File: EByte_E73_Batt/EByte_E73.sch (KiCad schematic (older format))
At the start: 14 parts, among them J1 USB_OTG, J2 Serial Connector, U1 E73-2G4M04S, U2 ProMicro, U3 AP2112K-3.3, U4 CP2102N-A01-GQFN24, U5 MCP73831-2-OT

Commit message: completed V2.0
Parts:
- removed U4: CP2102N-A01-GQFN24, Housings_DFN_QFN:QFN-24-1EP_4x4mm_Pitch0.5mm, symbol CP2102N-A01-GQFN24
- removed U5: MCP73831-2-OT, TO_SOT_Packages_SMD:SOT-23-5_HandSoldering, symbol MCP73831-2-OT
- added C5, C7, C8: 10uF, Capacitors_SMD:C_0805_HandSoldering, symbol C
- added C6: 1nF, Capacitors_SMD:C_0805_HandSoldering, symbol C
- added C9: 0.1uF, Capacitors_SMD:C_0805_HandSoldering, symbol C
- added D1: MBR120, Diodes_SMD:D_SOD-123, symbol MBR0520
- added J3: Conn_01x02, Pin_Headers:Pin_Header_Straight_1x02_Pitch2.54mm, symbol Conn_01x02
- added JP1: JUMPER-SMT_2_NO, E73:SolderJumperSingle, symbol JUMPER-SMT_2_NO
- added Q1: DMG3415U, TO_SOT_Packages_SMD:SOT-23, symbol BSS83P
- added R2: 100K, Resistors_SMD:R_0805_HandSoldering, symbol R
- added R3: 10K, Resistors_SMD:R_0805_HandSoldering, symbol R
- added R4: 806K, Resistors_SMD:R_0805_HandSoldering, symbol R
- added R5: 2M, Resistors_SMD:R_0805_HandSoldering, symbol R
- added R6: 1K, Resistors_SMD:R_0805_HandSoldering, symbol R
- added U4: CH340C, SMD_Packages:SO-16-N, symbol CH340C
- added U6: TP4056, Power_Integrations:SO-8, symbol TP4056
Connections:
- net labels added: DTR, Data+, Data-, VBatt, VBus
- wire segments 94 -> 156
- no-connect marks 2 -> 10
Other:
- note added: "LiPo Charging\n"
- note added: "Power and Filtering"
- moved on the sheet: J1, J2, R1, U3

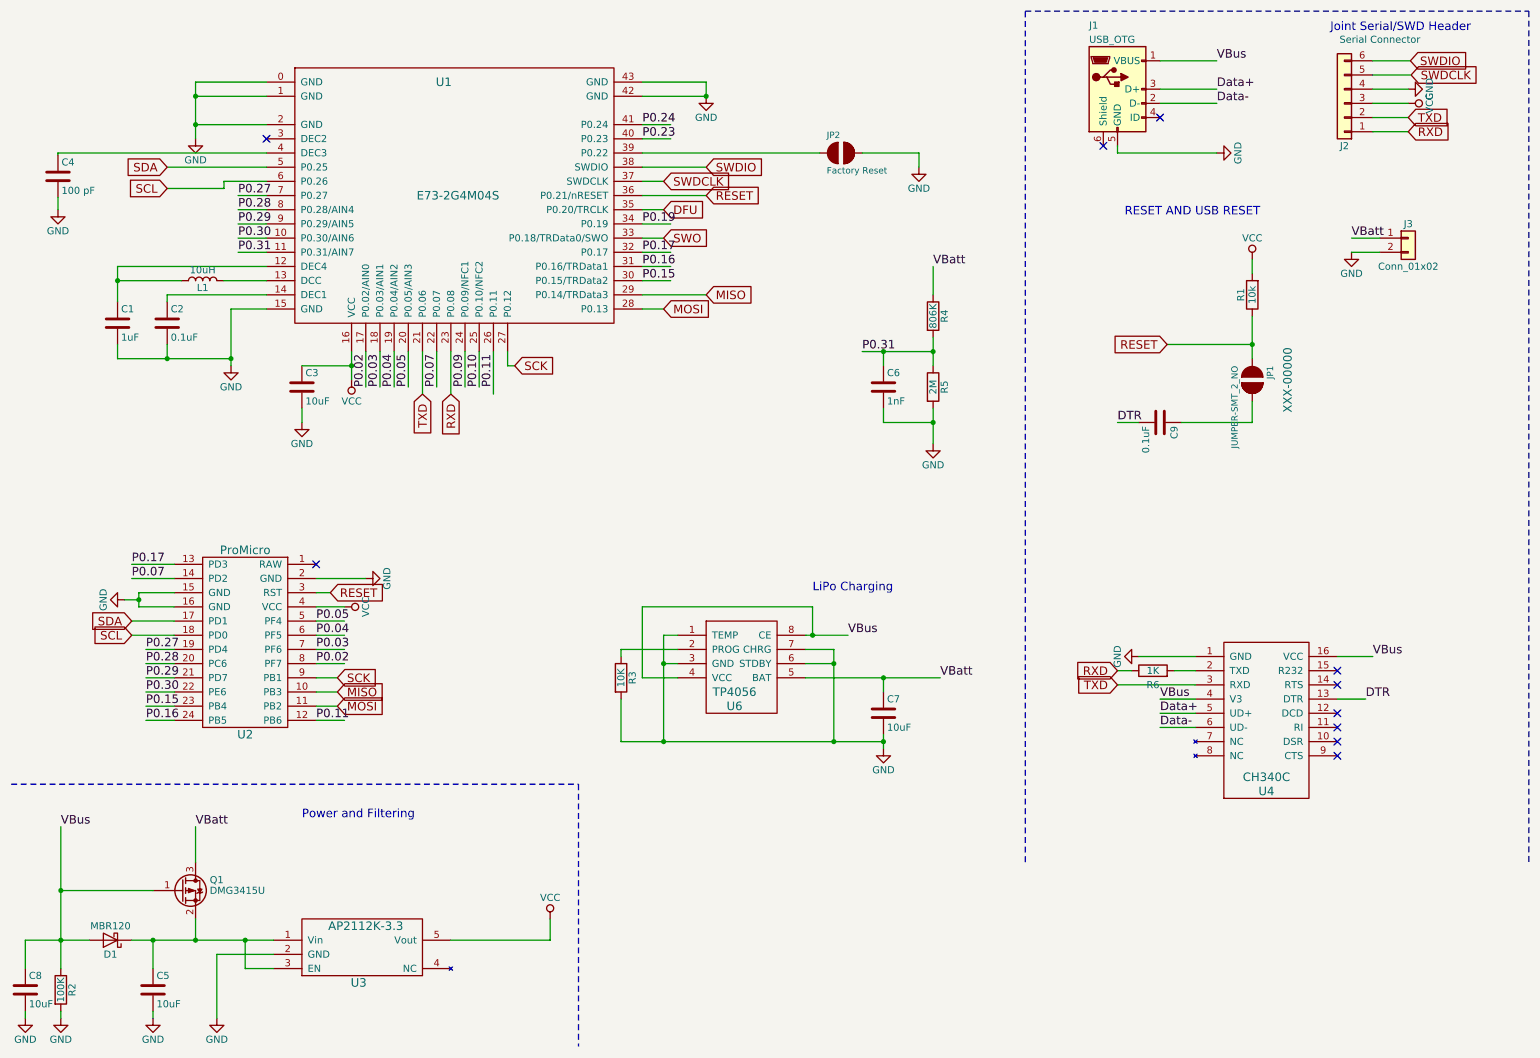
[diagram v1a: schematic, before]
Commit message: adding battery switch PCB
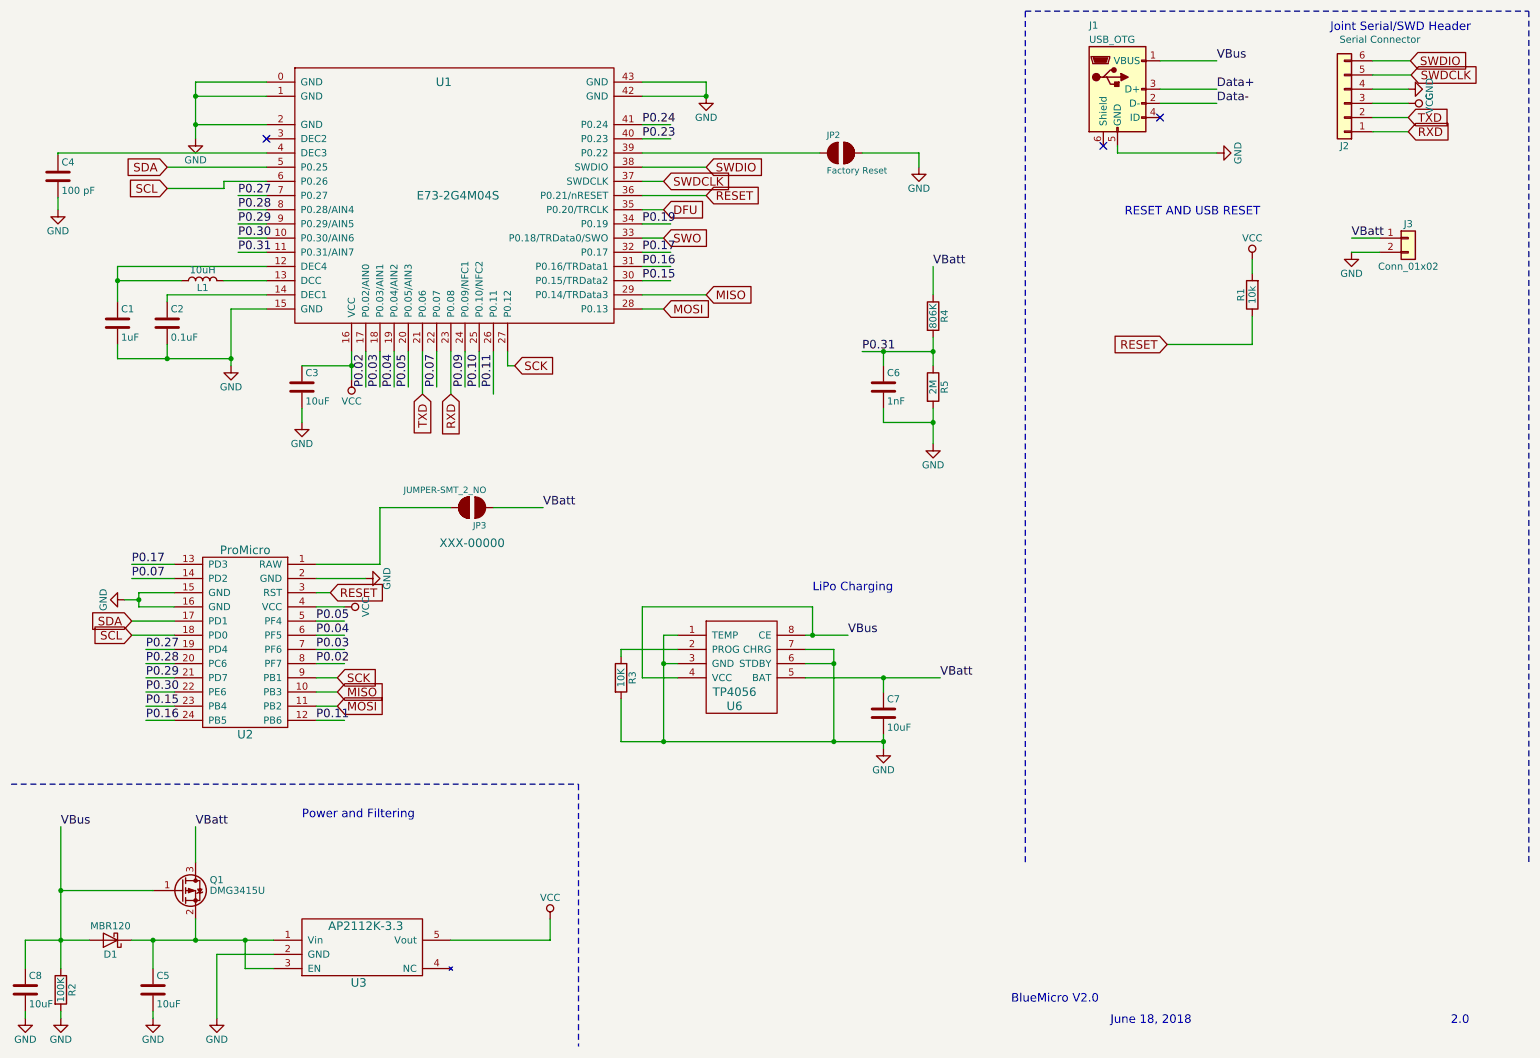
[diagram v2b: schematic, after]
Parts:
- removed C9: 0.1uF, Capacitors_SMD:C_0805_HandSoldering, symbol C
- removed JP1: JUMPER-SMT_2_NO, E73:SolderJumperSingle, symbol JUMPER-SMT_2_NO
- removed R6: 1K, Resistors_SMD:R_0805_HandSoldering, symbol R
- removed U4: CH340C, SMD_Packages:SO-16-N, symbol CH340C
- added JP3: JUMPER-SMT_2_NO, E73:SolderJumperSingle, symbol JUMPER-SMT_2_NO
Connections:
- net labels removed: DTR
- wire segments 156 -> 148
- no-connect marks 10 -> 3
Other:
- note added: "2.0"
- note added: "BlueMicro V2.0"
- note added: "June 18, 2018"
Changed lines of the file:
@@
 Wire Wire Line
 	2750 4600 2650 4600
-NoConn ~ 2650 4400
 Text GLabel 2800 5400 2    60   Input ~ 0
 MOSI
@@
 Text Label 9950 2100 0    60   ~ 0
 VBatt
-$Comp
-L R R6
-U 1 1 5B15C03B
-P 8550 5150
-F 0 "R6" V 8450 5150 50  0000 C CNN
-F 1 "1K" V 8550 5150 50  0000 C CNN
-F 2 "Resistors_SMD:R_0805_HandSoldering" V 8480 5150 50  0001 C CNN
-F 3 "" H 8550 5150 50  0001 C CNN
-	1    8550 5150
-	0    -1   -1   0
-$EndComp
-Text GLabel 8300 5150 0    60   Input ~ 0
-RXD
-Text GLabel 8300 5250 0    60   Input ~ 0
-TXD
 Text Label 6400 4900 0    60   ~ 0
 VBus
-$Comp
-L CH340C U4
-U 1 1 5B15E4EB
-P 9350 6150
-F 0 "U4" H 9350 6300 60  0000 C CNN
-F 1 "CH340C" H 9350 6400 60  0000 C CNN
-F 2 "SMD_Packages:SO-16-N" H 9350 6150 60  0001 C CNN
-F 3 "" H 9350 6150 60  0001 C CNN
-	1    9350 6150
-	1    0    0    -1
-$EndComp
-Wire Wire Line
-	9850 5350 10050 5350
-NoConn ~ 9850 5450
-NoConn ~ 9850 5550
-NoConn ~ 9850 5650
-NoConn ~ 9850 5750
-NoConn ~ 9850 5250
-$Comp
-L GND #PWR021
-U 1 1 5B15E785
-P 8450 5050
-F 0 "#PWR021" H 8450 4800 50  0001 C CNN
-F 1 "GND" H 8450 4900 50  0000 C CNN
-F 2 "" H 8450 5050 50  0001 C CNN
-F 3 "" H 8450 5050 50  0001 C CNN
-	1    8450 5050
-	0    1    1    0
-$EndComp
-Wire Wire Line
-	9850 5050 10100 5050
-Wire Wire Line
-	8850 5350 8600 5350
-Text Label 10100 5050 0    60   ~ 0
-VBus
-Text Label 8600 5350 0    60   ~ 0
-VBus
-Text Label 10050 5350 0    60   ~ 0
-DTR
-NoConn ~ 9850 5150
-Wire Wire Line
-	8850 5450 8600 5450
-Wire Wire Line
-	8850 5550 8600 5550
-Text Label 8600 5450 0    60   ~ 0
-Data+
-Text Label 8600 5550 0    60   ~ 0
-Data-
-Wire Wire Line
-	8300 5250 8850 5250
-Wire Wire Line
-	8850 5150 8700 5150
-Wire Wire Line
-	8400 5150 8300 5150
-Wire Wire Line
-	8450 5050 8850 5050
 $Comp
 L C C8
@@
 	600  7250 600  7050
 $Comp
-L C C9
-U 1 1 5B16084D
-P 8600 3400
-F 0 "C9" H 8625 3500 50  0000 L CNN
-F 1 "0.1uF" H 8625 3300 50  0000 L CNN
-F 2 "Capacitors_SMD:C_0805_HandSoldering" H 8638 3250 50  0001 C CNN
-F 3 "" H 8600 3400 50  0001 C CNN
-	1    8600 3400
-	0    1    1    0
-$EndComp
-Wire Wire Line
-	8450 3400 8300 3400
-Text Label 8300 3400 0    60   ~ 0
-DTR
-$Comp
-L JUMPER-SMT_2_NO JP1
-U 1 1 5B160FF4
-P 9250 3100
-F 0 "JP1" H 9150 3200 45  0000 L BNN
-F 1 "JUMPER-SMT_2_NO" H 9150 2950 45  0000 L BNN
-F 2 "E73:SolderJumperSingle" H 9250 3300 20  0001 C CNN
-F 3 "" H 9250 3100 60  0001 C CNN
-F 4 "XXX-00000" H 9250 3350 60  0000 C CNN "PROD_ID"
-	1    9250 3100
-	0    1    1    0
-$EndComp
-Wire Wire Line
-	9250 2650 9250 2950
-Wire Wire Line
-	8650 2850 9250 2850
-Connection ~ 9250 2850
-Wire Wire Line
-	8750 3400 9250 3400
-Wire Wire Line
-	9250 3400 9250 3250
-$Comp
 L TP4056 U6
 U 1 1 5B15E4E3
@@
 	6100 5000 6300 5000
 Wire Wire Line
-	6300 5000 6300 5650
+	6300 5650 6300 5000
 Wire Wire Line
 	4800 5650 6650 5650
@@
 Text Label 6500 2900 0    60   ~ 0
 P0.31
+$Comp
+L JUMPER-SMT_2_NO JP3
+U 1 1 5B23104A
+P 3750 4000
+F 0 "JP3" H 3650 4100 45  0000 L BNN
+F 1 "JUMPER-SMT_2_NO" H 3650 3850 45  0000 L BNN
+F 2 "E73:SolderJumperSingle" H 3750 4200 20  0001 C CNN
+F 3 "" H 3750 4000 60  0001 C CNN
+F 4 "XXX-00000" H 3750 4250 60  0000 C CNN "PROD_ID"
+	1    3750 4000
+	-1   0    0    1
+$EndComp
+Wire Wire Line
+	3600 4000 3100 4000
+Wire Wire Line
+	3100 4000 3100 4400
+Wire Wire Line
+	3100 4400 2650 4400
+Wire Wire Line
+	3900 4000 4250 4000
+Text Label 4250 4000 0    60   ~ 0
+VBatt
+Text Notes 7550 7500 0    60   ~ 0
+BlueMicro V2.0
+Text Notes 8250 7650 0    60   ~ 0
+June 18, 2018
+Text Notes 10650 7650 0    60   ~ 0
+2.0
+Wire Wire Line
+	9250 2650 9250 2850
+Wire Wire Line
+	9250 2850 8650 2850
 $EndSCHEMATC
